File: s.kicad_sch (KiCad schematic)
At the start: 29 parts, among them J2 UART connector, J5 USB4105-GF-A, SW26 210-4MS, U1 ESP32-S3-WROOM-1, U2 MCP1825S

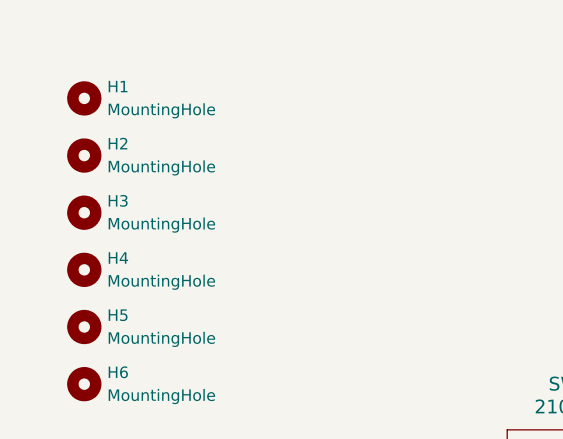
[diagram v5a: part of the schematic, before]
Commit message: add the fourth mounting hole
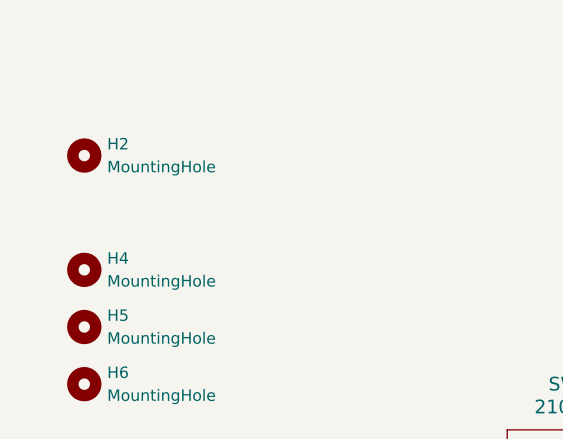
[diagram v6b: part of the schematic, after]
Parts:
- removed H1, H3: MountingHole, MountingHole:MountingHole_3mm, symbol Mechanical:MountingHole
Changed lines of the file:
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@@
-	)
-	(symbol
-		(lib_id "Mechanical:MountingHole")
-		(at 26.67 21.59 0)
-		(unit 1)
-		(exclude_from_sim no)
-		(in_bom no)
-		(on_board yes)
-		(dnp no)
-		(fields_autoplaced yes)
-		(property "Reference" "H1"
-			(at 29.21 20.3199 0)
-			(effects
-				(font
-					(size 1.27 1.27)
-				)
-				(justify left)
-			)
-		)
-		(property "Value" "MountingHole"
-			(at 29.21 22.8599 0)
-			(effects
-				(font
-					(size 1.27 1.27)
-				)
-				(justify left)
-			)
-		)
-		(property "Footprint" "MountingHole:MountingHole_3mm"
-			(at 26.67 21.59 0)
-			(effects
-				(font
-					(size 1.27 1.27)
-				)
-				(hide yes)
-			)
-		)
-		(property "Datasheet" "~"
-			(at 26.67 21.59 0)
-			(effects
-				(font
-					(size 1.27 1.27)
-				)
-				(hide yes)
-			)
-		)
-		(property "Description" "Mounting Hole without connection"
-			(at 26.67 21.59 0)
-			(effects
-				(font
-					(size 1.27 1.27)
-				)
-				(hide yes)
-			)
-		)
-		(instances
-			(project ""
-				(path "/915d30bc-a319-49d8-8691-e2837c0e16bd"
-					(reference "H1")
-					(unit 1)
-				)
-			)
-		)
 	)
 	(symbol
@@
 					(unit 1)
 				)
-			)
-		)
-	)
-	(symbol
-		(lib_id "Mechanical:MountingHole")
-		(at 26.67 34.29 0)
-		(unit 1)
-		(exclude_from_sim no)
-		(in_bom no)
-		(on_board yes)
-		(dnp no)
-		(fields_autoplaced yes)
-		(property "Reference" "H3"
-			(at 29.21 33.0199 0)
-			(effects
-				(font
-					(size 1.27 1.27)
-				)
-				(justify left)
-			)
-		)
-		(property "Value" "MountingHole"
-			(at 29.21 35.5599 0)
-			(effects
-				(font
-					(size 1.27 1.27)
-				)
-				(justify left)
-			)
-		)
-		(property "Footprint" "MountingHole:MountingHole_3mm"
-			(at 26.67 34.29 0)
-			(effects
-				(font
-					(size 1.27 1.27)
-				)
-				(hide yes)
-			)
-		)
-		(property "Datasheet" "~"
-			(at 26.67 34.29 0)
-			(effects
-				(font
-					(size 1.27 1.27)
-				)
-				(hide yes)
-			)
-		)
-		(property "Description" "Mounting Hole without connection"
-			(at 26.67 34.29 0)
-			(effects
-				(font
-					(size 1.27 1.27)
-				)
-				(hide yes)
-			)
-		)
-		(instances
-			(project "s"
-				(path "/915d30bc-a319-49d8-8691-e2837c0e16bd"
-					(reference "H3")
-					(unit 1)
-				)

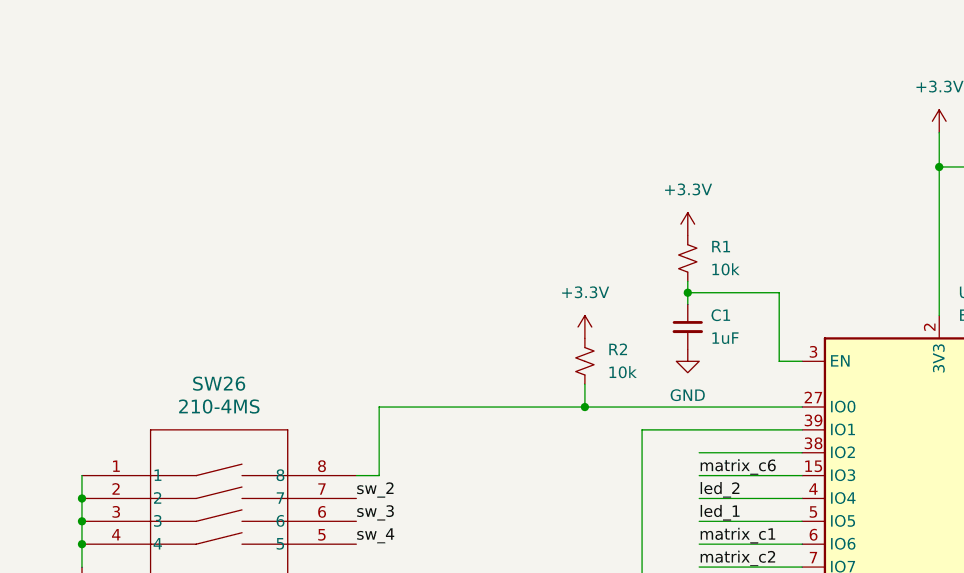
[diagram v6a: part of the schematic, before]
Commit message: add a push button for RST
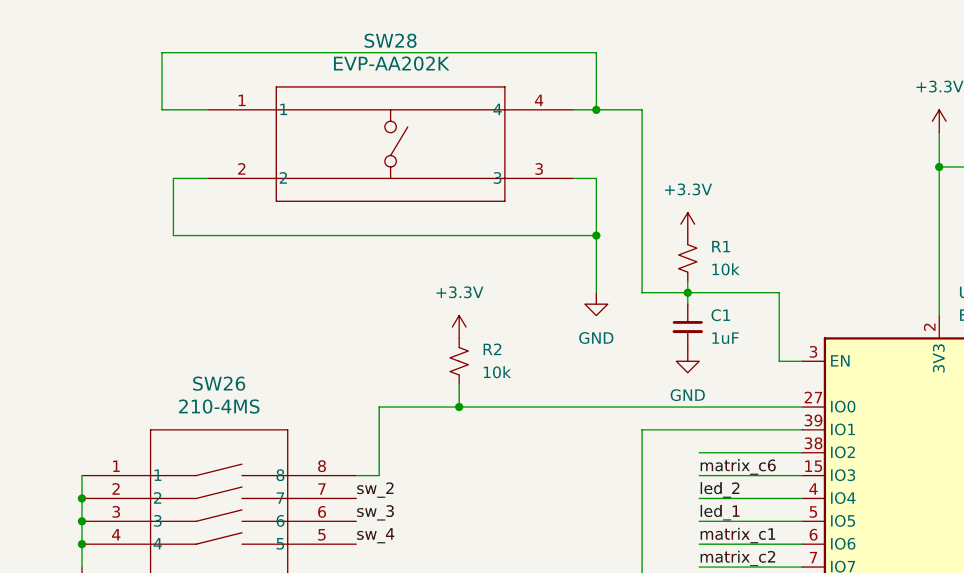
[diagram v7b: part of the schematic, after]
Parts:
- added SW28: EVP-AA202K, SW_EVP-AA102K_PAN, symbol push_btn_aa202k:EVP-AA202K
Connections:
- net GND: now also SW28.2, SW28.3
- net at C1.1, R1.2, U1.3 (EN): now also SW28.1, SW28.4
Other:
- moved on the sheet: R2

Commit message: change footprint of JST connector. Vertical -> horizontal
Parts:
- SW28: footprint SW_EVP-AA102K_PAN -> push_btn_aa202k:SW_EVP-AA102K_PAN
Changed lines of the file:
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@@
 			)
 		)
-		(property "Footprint" "SW_EVP-AA102K_PAN"
+		(property "Footprint" "push_btn_aa202k:SW_EVP-AA102K_PAN"
 			(at 80.01 22.86 0)
 			(effects
